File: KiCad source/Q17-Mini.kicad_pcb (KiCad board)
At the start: 2 copper layers, 95 x 75 mm, 85 parts, among them J1 Input, Q1 FQP3N30, Q10 KSA992, Q11 BS250P, Q12 BD139, Q13 FQP3N30, Q14 IRF9610, Q15 FQA46N15, Q16 FQA36P15, Q2 KSA992, Q3 KSC1845, Q4 FQP3P20, Q5 FQP3P20, Q6 FQP3N30, Q7 KSC1845, Q8 2N7000, Q9 BS250P, U1 OPA1641

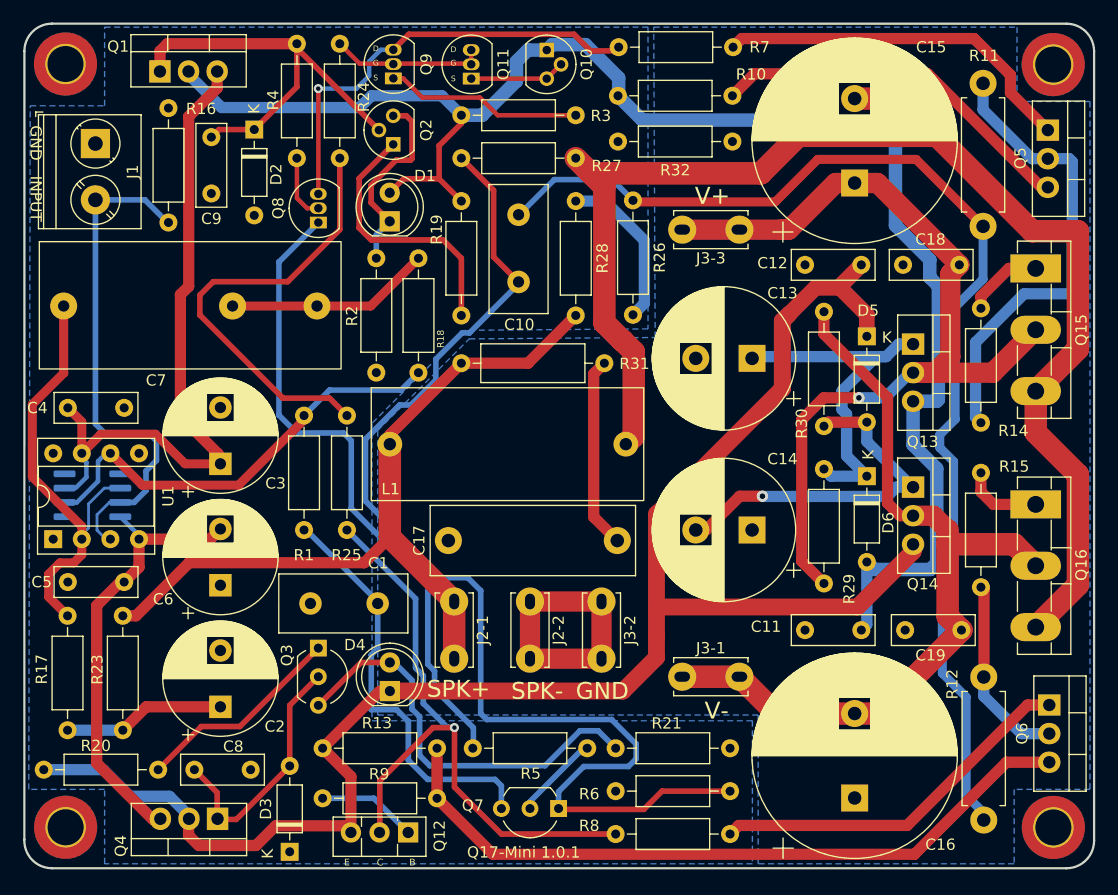
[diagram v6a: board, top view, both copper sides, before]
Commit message: PCB version 1.0.2
- New footprint for C17 with lead space of 10mm.
- Moved some track.
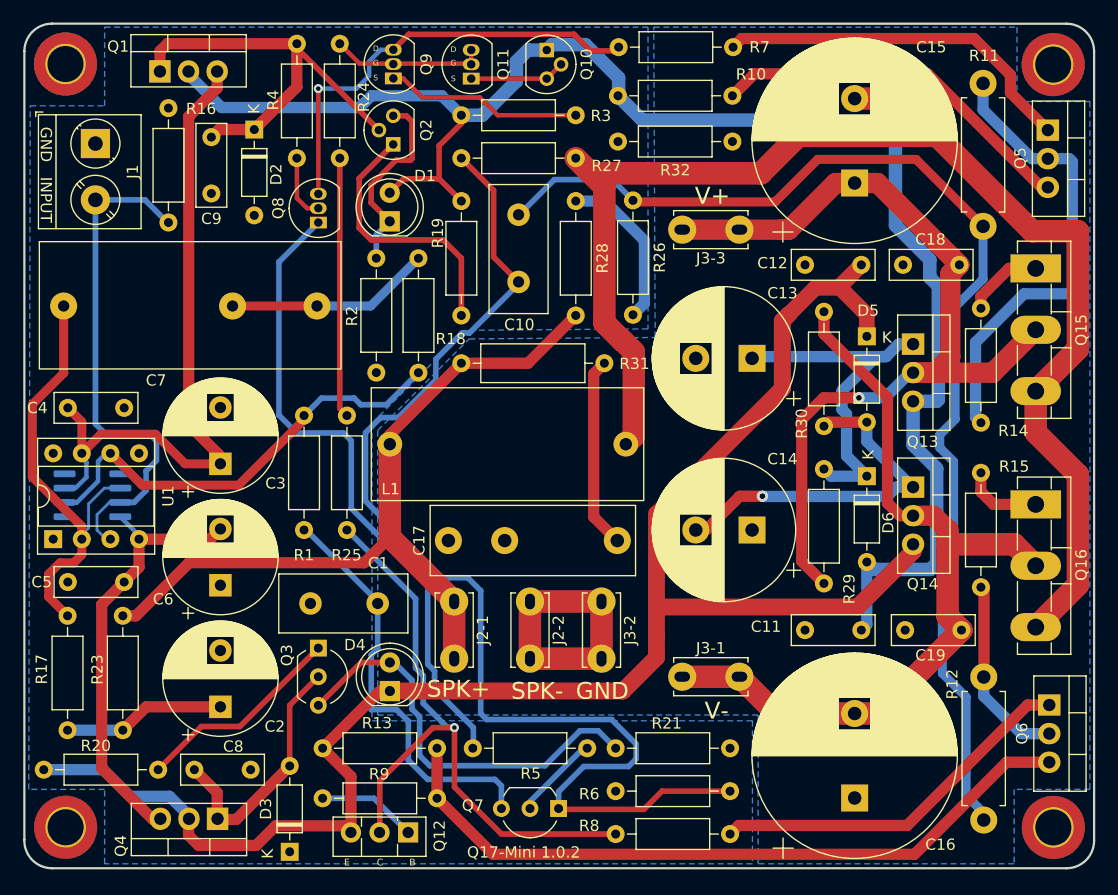
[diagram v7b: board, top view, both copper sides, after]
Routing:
- net Net-(R24-Pad2): track 39.7 -> 23.1 mm
- net Net-(C3-Pad1): track 60.1 -> 59.5 mm
- net Net-(C5-Pad2): track 39.5 -> 38.9 mm
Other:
- board text added: "Q17-Mini 1.0.2"
- board text removed: "Q17-Mini 1.0.1"

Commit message: PCB v1.0.3
Changed footprint for Q2, Q9, Q10 and Q11.
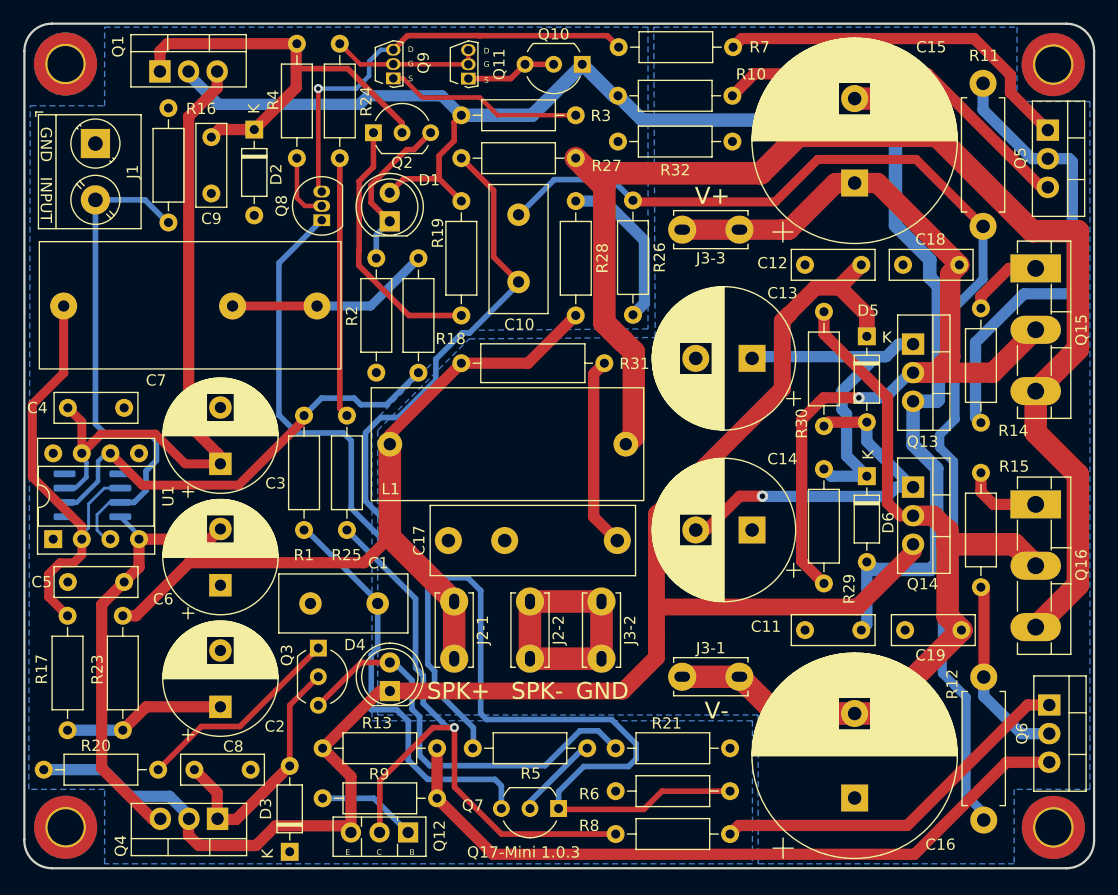
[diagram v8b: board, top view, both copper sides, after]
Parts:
- Q10, Q2: footprint Package_TO_SOT_THT:TO-92 -> Package_TO_SOT_THT:TO-92_Inline_Wide
- Q11, Q9: footprint Package_TO_SOT_THT:TO-92_Inline -> Package_TO_SOT_THT:TO-92S
- moved Q10 3.40 mm to (149.4, 58.7), turned to 180 degrees
- moved Q2 2.04 mm to (130.8, 64.7), turned to 0 degrees
- moved Q8 0.36 mm to (126.2, 72.5)
- moved Q11 0.25 mm to (139.2, 59.9)
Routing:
- net Net-(C11-Pad2): track 149.7 -> 146.2 mm
- net Net-(D1-Pad1): track 17.5 -> 14.9 mm
- net Net-(C9-Pad2): track 38.0 -> 39.7 mm
- net Net-(Q2-Pad1): track 23.9 -> 23.3 mm
- net Net-(Q10-Pad2): track 8.50 -> 7.85 mm
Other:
- board text added: "Q17-Mini 1.0.3"
- board text removed: "Q17-Mini 1.0.2"
